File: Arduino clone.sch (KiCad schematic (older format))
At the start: 13 parts, among them U1 24LC1025, U2 24LC1025, U3 DS1337S+, U4 ATMEGA328P-AU, Y1 Crystal 32MHz, Y2 Crystal 16MHz

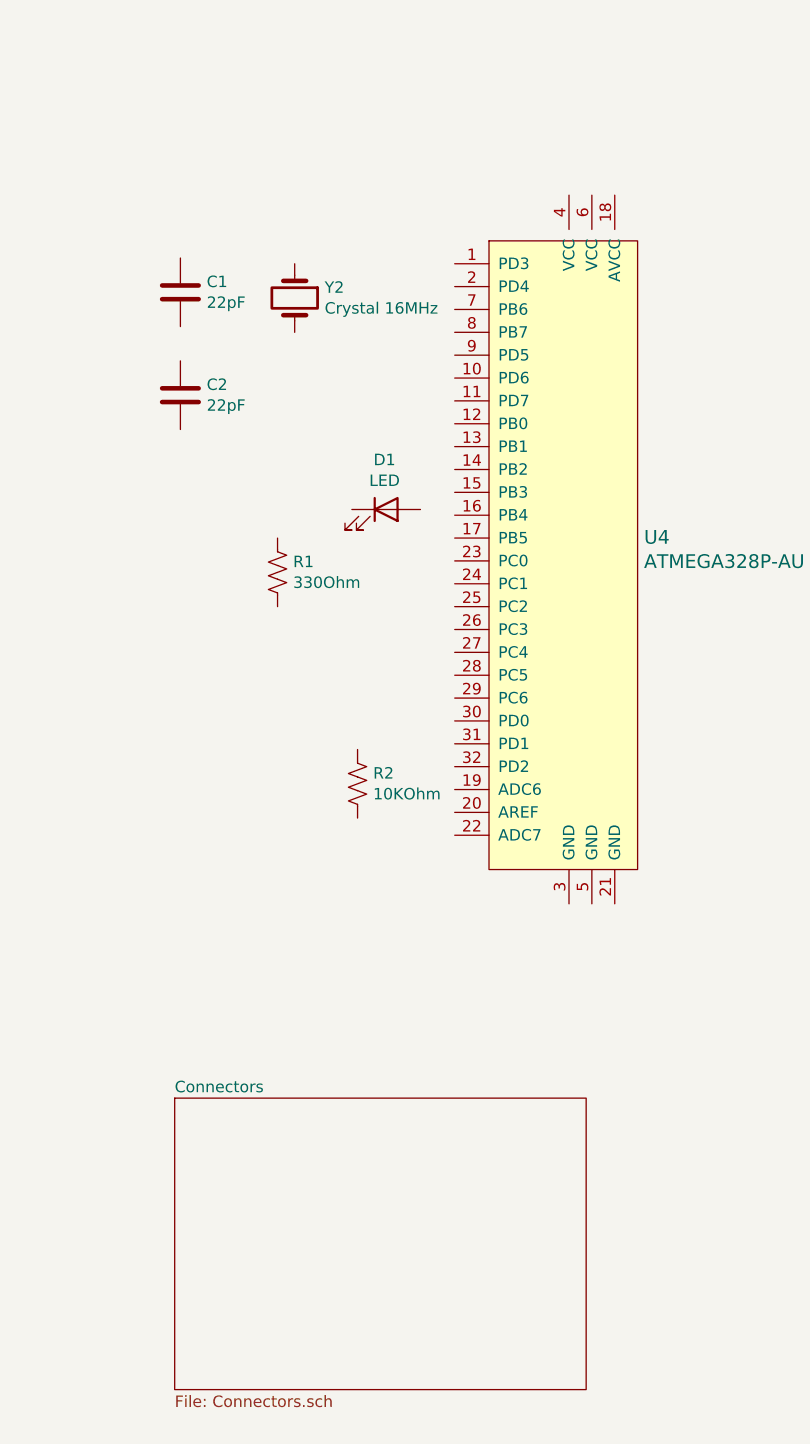
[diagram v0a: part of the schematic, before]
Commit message: Added hierarchical labels
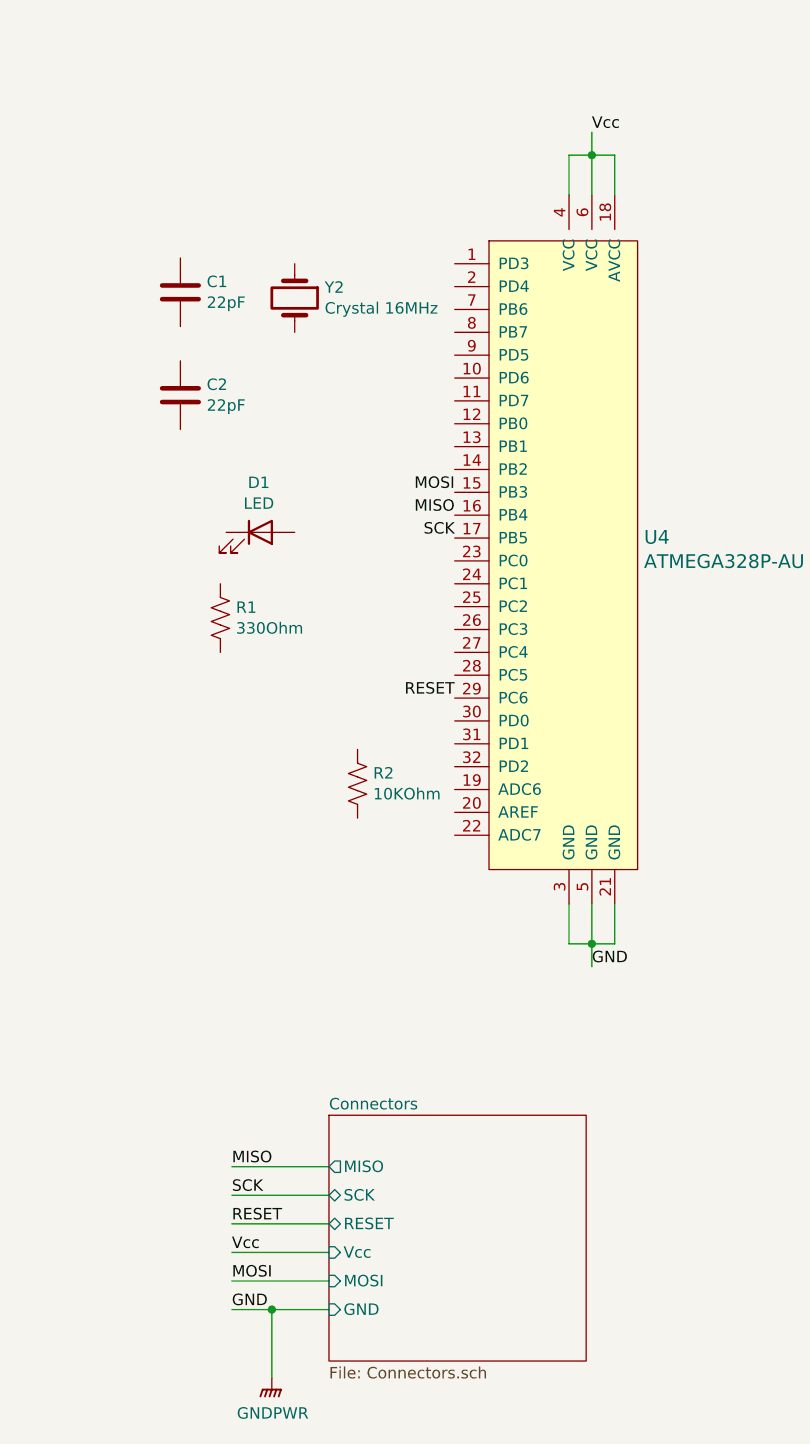
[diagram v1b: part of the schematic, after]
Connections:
- net GND: now also U4.21 (GND), U4.3 (GND), U4.5 (GND)
- net MOSI: now reaches U4.15 (PB3)
- net MISO: now reaches U4.16 (PB4)
- net SCK: now reaches U4.17 (PB5)
- net Vcc: now reaches U4.18 (AVCC)
- net Vcc: now also U4.4 (VCC), U4.6 (VCC)
- net RESET: now reaches U4.29 (PC6)
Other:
- moved on the sheet: D1, R1
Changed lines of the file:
@@
 L Device:R_US R1
 U 1 1 601B6694
-P 5125 3725
-F 0 "R1" H 5193 3771 50  0000 L CNN
-F 1 "330Ohm" H 5193 3680 50  0000 L CNN
-F 2 "Resistor_SMD:R_0805_2012Metric_Pad1.20x1.40mm_HandSolder" V 5165 3715 50  0001 C CNN
-F 3 "~" H 5125 3725 50  0001 C CNN
-	1    5125 3725
+P 4875 3925
+F 0 "R1" H 4943 3971 50  0000 L CNN
+F 1 "330Ohm" H 4943 3880 50  0000 L CNN
+F 2 "Resistor_SMD:R_0805_2012Metric_Pad1.20x1.40mm_HandSolder" V 4915 3915 50  0001 C CNN
+F 3 "~" H 4875 3925 50  0001 C CNN
+	1    4875 3925
 	1    0    0    -1
 $EndComp
@@
 	1    0    0    -1
 $EndComp
+$Comp
+L Device:Crystal Y1
+U 1 1 601C298C
+P 1225 2250
+F 0 "Y1" H 1225 2518 50  0000 C CNN
+F 1 "Crystal 32MHz" H 1225 2427 50  0000 C CNN
+F 2 "Crystal:Crystal_SMD_MicroCrystal_CC7V-T1A-2Pin_3.2x1.5mm_HandSoldering" H 1225 2250 50  0001 C CNN
+F 3 "~" H 1225 2250 50  0001 C CNN
+	1    1225 2250
+	1    0    0    -1
+$EndComp
+$Comp
+L Device:Crystal Y2
+U 1 1 601C36A9
+P 5200 2525
+F 0 "Y2" V 5154 2656 50  0000 L CNN
+F 1 "Crystal 16MHz" V 5245 2656 50  0000 L CNN
+F 2 "Crystal:Crystal_SMD_5032-2Pin_5.0x3.2mm_HandSoldering" H 5200 2525 50  0001 C CNN
+F 3 "~" H 5200 2525 50  0001 C CNN
+	1    5200 2525
+	0    1    1    0
+$EndComp
+$Comp
+L power:GND #PWR01
+U 1 1 601D629C
+P 9525 2525
+F 0 "#PWR01" H 9525 2275 50  0001 C CNN
+F 1 "GND" H 9530 2352 50  0000 C CNN
+F 2 "" H 9525 2525 50  0001 C CNN
+F 3 "" H 9525 2525 50  0001 C CNN
+	1    9525 2525
+	1    0    0    -1
+$EndComp
+$Comp
+L Memory_EEPROM:24LC1025 U2
+U 1 1 601CAEF5
+P 2400 5400
+F 0 "U2" H 2400 5881 50  0000 C CNN
+F 1 "24LC1025" H 2400 5790 50  0000 C CNN
+F 2 "Package_SO:SOIJ-8_5.3x5.3mm_P1.27mm" H 2400 5400 50  0001 C CNN
+F 3 "http://ww1.microchip.com/downloads/en/DeviceDoc/21941B.pdf" H 2400 5400 50  0001 C CNN
+	1    2400 5400
+	1    0    0    -1
+$EndComp
+$Comp
+L Abtahi's_Library:DS1337_AM U3
+U 1 1 601C4304
+P 2525 2450
+F 0 "U3" H 2525 3256 50  0000 C CNN
+F 1 "DS1337S+" H 2525 3165 50  0000 C CNN
+F 2 "Package_SO:SO-8_5.3x6.2mm_P1.27mm" H 2525 2450 50  0001 C CNN
+F 3 "" H 2525 2450 50  0001 C CNN
+	1    2525 2450
+	1    0    0    -1
+$EndComp
+$Comp
+L Memory_EEPROM:24LC1025 U1
+U 1 1 601B7371
+P 2400 6450
+F 0 "U1" H 2400 6931 50  0000 C CNN
+F 1 "24LC1025" H 2400 6840 50  0000 C CNN
+F 2 "Package_SO:SOIJ-8_5.3x5.3mm_P1.27mm" H 2400 6450 50  0001 C CNN
+F 3 "http://ww1.microchip.com/downloads/en/DeviceDoc/21941B.pdf" H 2400 6450 50  0001 C CNN
+	1    2400 6450
+	1    0    0    -1
+$EndComp
+$Comp
+L Device:LED D1
+U 1 1 601B5CCB
+P 5050 3550
+F 0 "D1" H 5043 3767 50  0000 C CNN
+F 1 "LED" H 5043 3676 50  0000 C CNN
+F 2 "LED_SMD:LED_0805_2012Metric_Pad1.15x1.40mm_HandSolder" H 5050 3550 50  0001 C CNN
+F 3 "~" H 5050 3550 50  0001 C CNN
+	1    5050 3550
+	1    0    0    -1
+$EndComp
+Text Label 4925 6325 0    50   ~ 0
+MISO
+Wire Wire Line
+	4925 6325 5350 6325
+Text Label 5900 3475 2    50   ~ 0
+MISO
+Text Label 4925 6450 0    50   ~ 0
+SCK
+Text Label 4925 6575 0    50   ~ 0
+RESET
+Text Label 4925 6700 0    50   ~ 0
+Vcc
+Text Label 4925 6825 0    50   ~ 0
+MOSI
+Text Label 4925 6950 0    50   ~ 0
+GND
+Wire Wire Line
+	4925 6450 5350 6450
+Wire Wire Line
+	4925 6575 5350 6575
+Wire Wire Line
+	4925 6700 5350 6700
+Wire Wire Line
+	4925 6825 5350 6825
+Wire Wire Line
+	4925 6950 5100 6950
+Text Label 5900 3575 2    50   ~ 0
+SCK
+$Sheet
+S 5350 6100 1125 1075
+U 601B8BF2
+F0 "Connectors" 50
+F1 "Connectors.sch" 50
+F2 "MISO" O L 5350 6325 50
+F3 "SCK" B L 5350 6450 50
+F4 "RESET" B L 5350 6575 50
+F5 "Vcc" I L 5350 6700 50
+F6 "MOSI" I L 5350 6825 50
+F7 "GND" I L 5350 6950 50
+$EndSheet
+Text Label 5900 3375 2    50   ~ 0
+MOSI
+Text Label 5900 4275 2    50   ~ 0
+RESET
+Wire Wire Line
+	6400 2075 6400 1900
+Wire Wire Line
+	6400 1900 6500 1900
+Wire Wire Line
+	6500 2075 6500 1900
+Wire Wire Line
+	6600 2075 6600 1900
+Wire Wire Line
+	6600 1900 6500 1900
+Connection ~ 6500 1900
+Text Label 6500 5450 0    50   ~ 0
+GND
+Text Label 6500 1800 0    50   ~ 0
+Vcc
+Wire Wire Line
+	6500 1800 6500 1900
 $Comp
 L dk_Embedded-Microcontrollers:ATMEGA328P-AU U4
@@
 	1    0    0    -1
 $EndComp
-$Comp
-L Device:Crystal Y1
-U 1 1 601C298C
-P 1225 2250
-F 0 "Y1" H 1225 2518 50  0000 C CNN
-F 1 "Crystal 32MHz" H 1225 2427 50  0000 C CNN
-F 2 "Crystal:Crystal_SMD_MicroCrystal_CC7V-T1A-2Pin_3.2x1.5mm_HandSoldering" H 1225 2250 50  0001 C CNN
-F 3 "~" H 1225 2250 50  0001 C CNN
-	1    1225 2250
-	1    0    0    -1
-$EndComp
-$Comp
-L Device:Crystal Y2
-U 1 1 601C36A9
-P 5200 2525
-F 0 "Y2" V 5154 2656 50  0000 L CNN
-F 1 "Crystal 16MHz" V 5245 2656 50  0000 L CNN
-F 2 "Crystal:Crystal_SMD_5032-2Pin_5.0x3.2mm_HandSoldering" H 5200 2525 50  0001 C CNN
-F 3 "~" H 5200 2525 50  0001 C CNN
-	1    5200 2525
-	0    1    1    0
-$EndComp
-$Comp
-L power:GND #PWR01
-U 1 1 601D629C
-P 9525 2525
-F 0 "#PWR01" H 9525 2275 50  0001 C CNN
-F 1 "GND" H 9530 2352 50  0000 C CNN
-F 2 "" H 9525 2525 50  0001 C CNN
-F 3 "" H 9525 2525 50  0001 C CNN
-	1    9525 2525
-	1    0    0    -1
-$EndComp
-$Comp
-L Memory_EEPROM:24LC1025 U2
-U 1 1 601CAEF5
-P 2400 5400
-F 0 "U2" H 2400 5881 50  0000 C CNN
-F 1 "24LC1025" H 2400 5790 50  0000 C CNN
-F 2 "Package_SO:SOIJ-8_5.3x5.3mm_P1.27mm" H 2400 5400 50  0001 C CNN
-F 3 "http://ww1.microchip.com/downloads/en/DeviceDoc/21941B.pdf" H 2400 5400 50  0001 C CNN
-	1    2400 5400
-	1    0    0    -1
-$EndComp
-$Comp
-L Abtahi's_Library:DS1337_AM U3
-U 1 1 601C4304
-P 2525 2450
-F 0 "U3" H 2525 3256 50  0000 C CNN
-F 1 "DS1337S+" H 2525 3165 50  0000 C CNN
-F 2 "Package_SO:SO-8_5.3x6.2mm_P1.27mm" H 2525 2450 50  0001 C CNN
-F 3 "" H 2525 2450 50  0001 C CNN
-	1    2525 2450
-	1    0    0    -1
-$EndComp
-$Comp
-L Memory_EEPROM:24LC1025 U1
-U 1 1 601B7371
-P 2400 6450
-F 0 "U1" H 2400 6931 50  0000 C CNN
-F 1 "24LC1025" H 2400 6840 50  0000 C CNN
-F 2 "Package_SO:SOIJ-8_5.3x5.3mm_P1.27mm" H 2400 6450 50  0001 C CNN
-F 3 "http://ww1.microchip.com/downloads/en/DeviceDoc/21941B.pdf" H 2400 6450 50  0001 C CNN
-	1    2400 6450
-	1    0    0    -1
-$EndComp
-$Comp
-L Device:LED D1
-U 1 1 601B5CCB
-P 5600 3450
-F 0 "D1" H 5593 3667 50  0000 C CNN
-F 1 "LED" H 5593 3576 50  0000 C CNN
-F 2 "LED_SMD:LED_0805_2012Metric_Pad1.15x1.40mm_HandSolder" H 5600 3450 50  0001 C CNN
-F 3 "~" H 5600 3450 50  0001 C CNN
-	1    5600 3450
-	1    0    0    -1
-$EndComp
-$Sheet
-S 4675 6025 1800 1275
-U 601B8BF2
-F0 "Connectors" 50
-F1 "Connectors.sch" 50
-$EndSheet
+Wire Wire Line
+	6400 5175 6400 5350
+Wire Wire Line
+	6600 5350 6600 5175
+Wire Wire Line
+	6400 5350 6500 5350
+Wire Wire Line
+	6500 5175 6500 5350
+Connection ~ 6500 5350
+Wire Wire Line
+	6500 5350 6600 5350
+Wire Wire Line
+	6500 5350 6500 5450
+$Comp
+L power:GNDPWR #PWR?
+U 1 1 602FDDD7
+P 5100 7250
+F 0 "#PWR?" H 5100 7050 50  0001 C CNN
+F 1 "GNDPWR" H 5104 7096 50  0000 C CNN
+F 2 "" H 5100 7200 50  0001 C CNN
+F 3 "" H 5100 7200 50  0001 C CNN
+	1    5100 7250
+	1    0    0    -1
+$EndComp
+Wire Wire Line
+	5100 7250 5100 6950
+Connection ~ 5100 6950
+Wire Wire Line
+	5100 6950 5350 6950
 $EndSCHEMATC

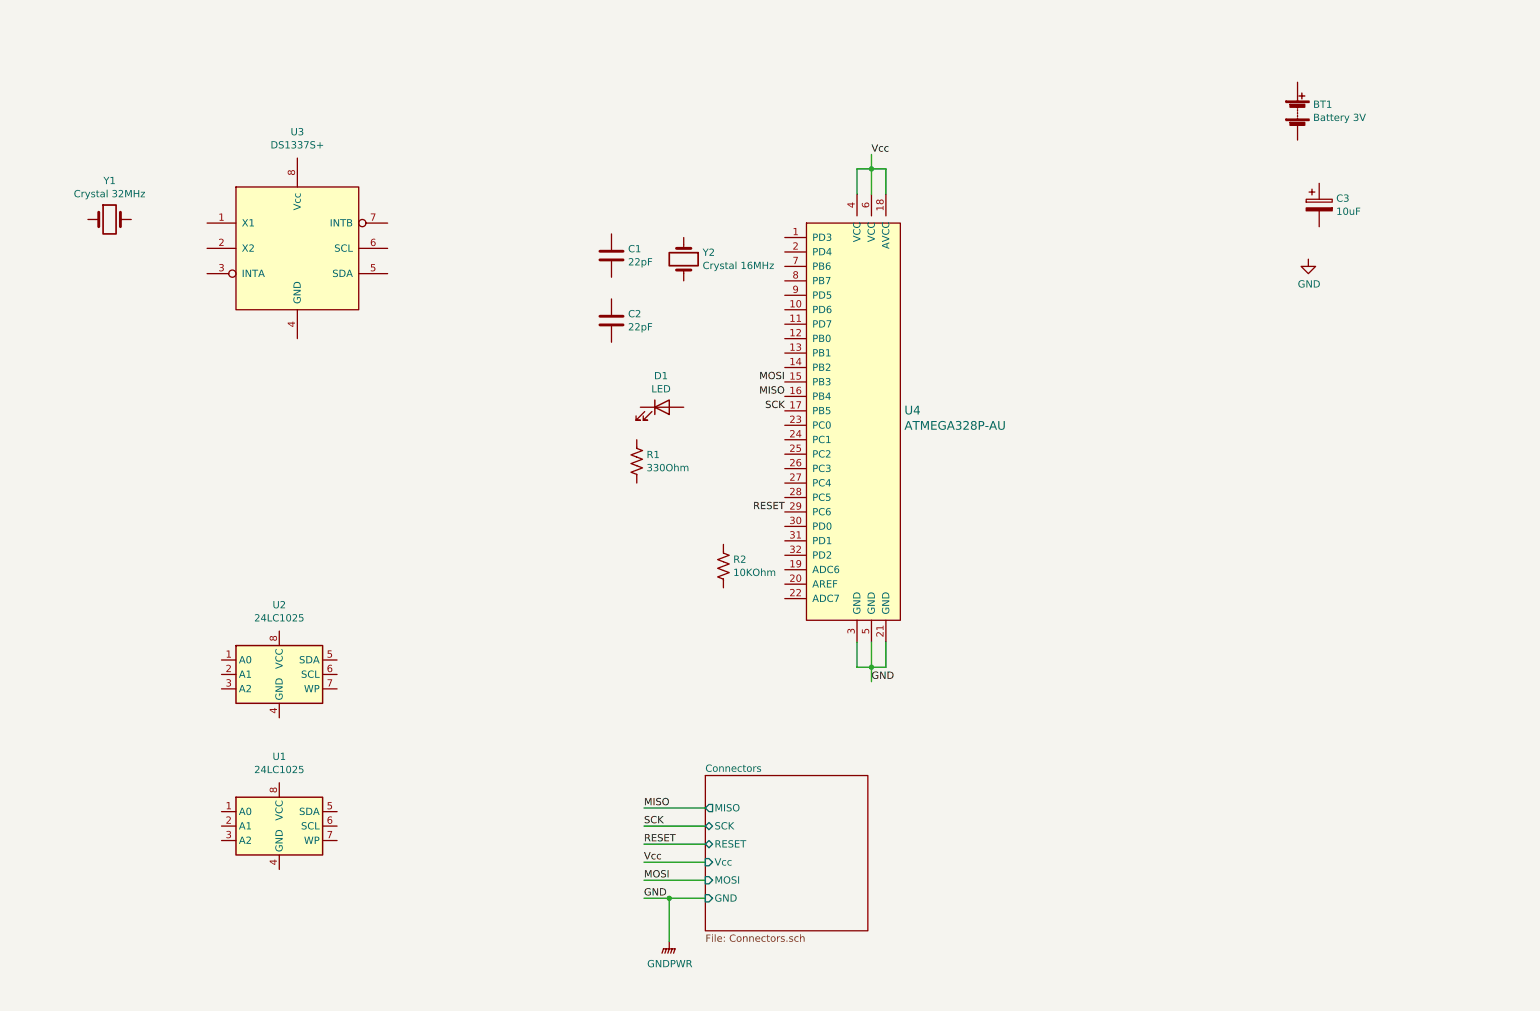
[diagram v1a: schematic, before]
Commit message: Finished hierarchical labels and root sheet connections
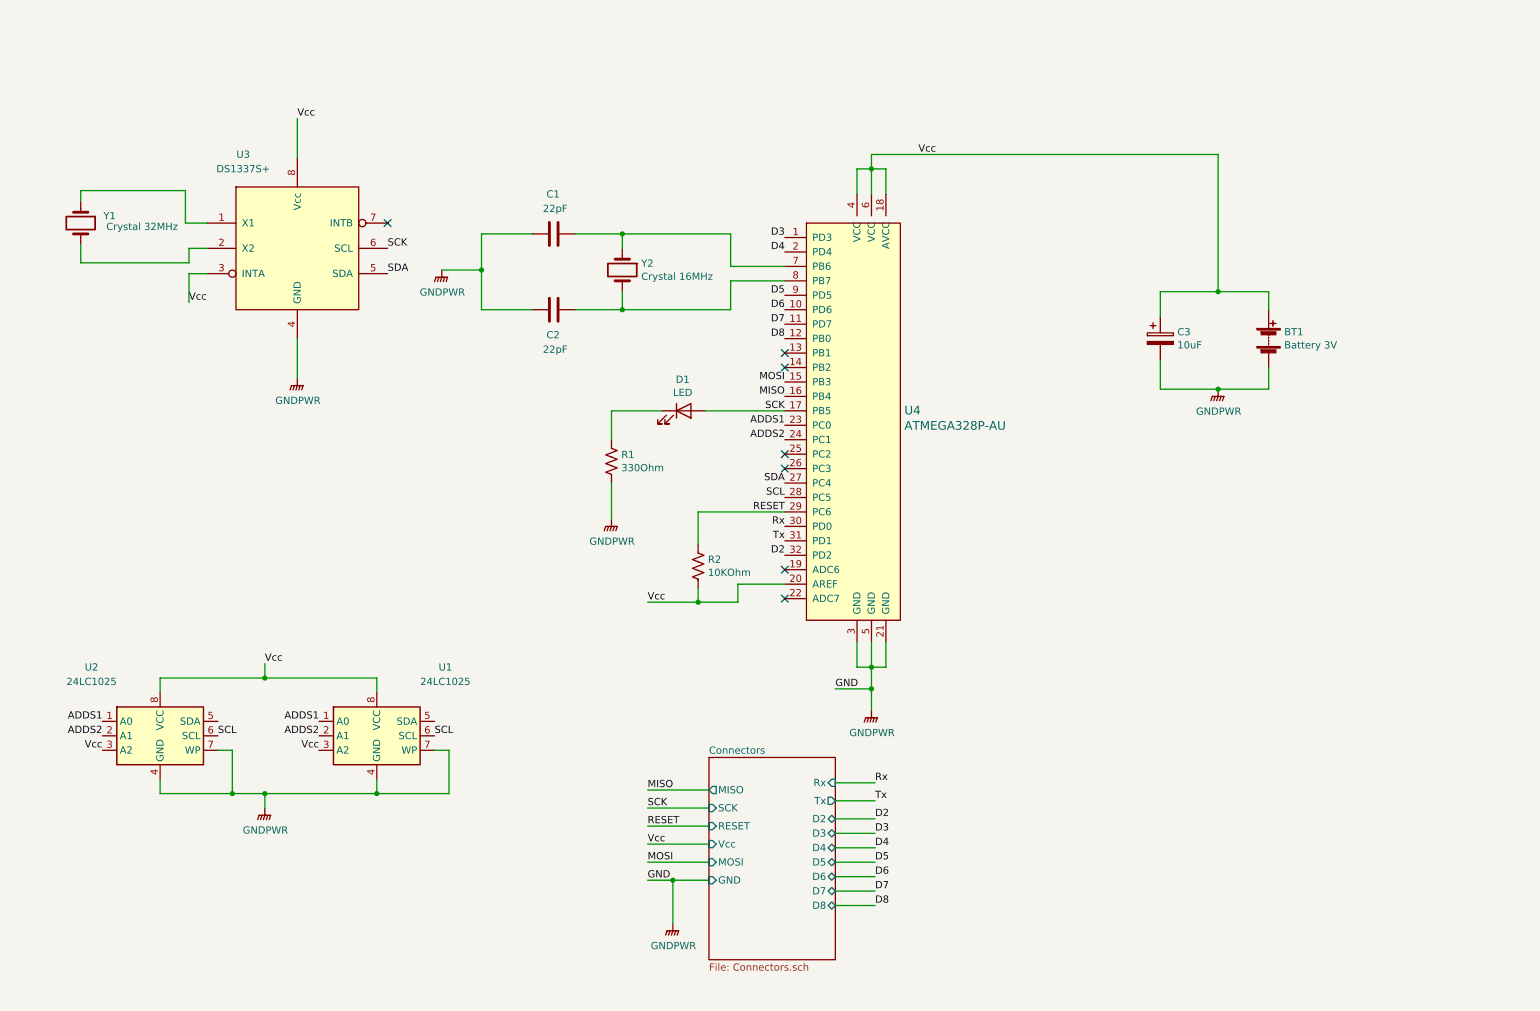
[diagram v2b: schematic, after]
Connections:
- net GND is gone; now on net GNDPWR: U4.21 (GND), U4.3 (GND), U4.5 (GND)
- net RESET: now also R2.1
- net SCK: now also D1.2 (A), U3.6 (SCL)
- net Vcc: now also BT1.1 (+), C3.1, R2.2, U1.3 (A2), U1.8 (VCC), U2.3 (A2), U2.8 (VCC), U3.3 (INTA), U3.8 (Vcc), U4.20 (AREF)
- net GNDPWR: now reaches BT1.2 (-)
- net GNDPWR: now also C1.2, C2.2, C3.2, R1.2, U1.4 (GND), U1.7 (WP), U2.4 (GND), U2.7 (WP), U3.4 (GND)
- net at C1.1: now also U4.7 (PB6), Y2.1
- net at C2.1: now also U4.8 (PB7), Y2.2
- net at D1.1 (K): now also R1.1
- net ADDS1: now reaches U1.1 (A0)
- net ADDS1: now also U2.1 (A0), U4.23 (PC0)
- net ADDS2: now reaches U1.2 (A1)
- net ADDS2: now also U2.2 (A1), U4.24 (PC1)
- net SCL: now reaches U1.6 (SCL)
- net SCL: now also U2.6 (SCL), U4.28 (PC5)
- net D3: now reaches U4.1 (PD3)
- net D6: now reaches U4.10 (PD6)
- net D7: now reaches U4.11 (PD7)
- net D8: now reaches U4.12 (PB0)
- net D4: now reaches U4.2 (PD4)
- net SDA: now reaches U4.27 (PC4)
- net SDA: now also U3.5 (SDA)
- net Rx: now reaches U4.30 (PD0)
- net Tx: now reaches U4.31 (PD1)
- net D2: now reaches U4.32 (PD2)
- net D5: now reaches U4.9 (PD5)
- net at Y1.1: now also U3.1 (X1)
- net at Y1.2: now also U3.2 (X2)
- no-connect marks 0 -> 7
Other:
- moved on the sheet: BT1, C1, C2, C3, D1, R1, R2, U1, U2, Y1, Y2
